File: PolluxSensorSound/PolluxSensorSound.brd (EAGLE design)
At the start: 100 x 80 mm, 0 parts

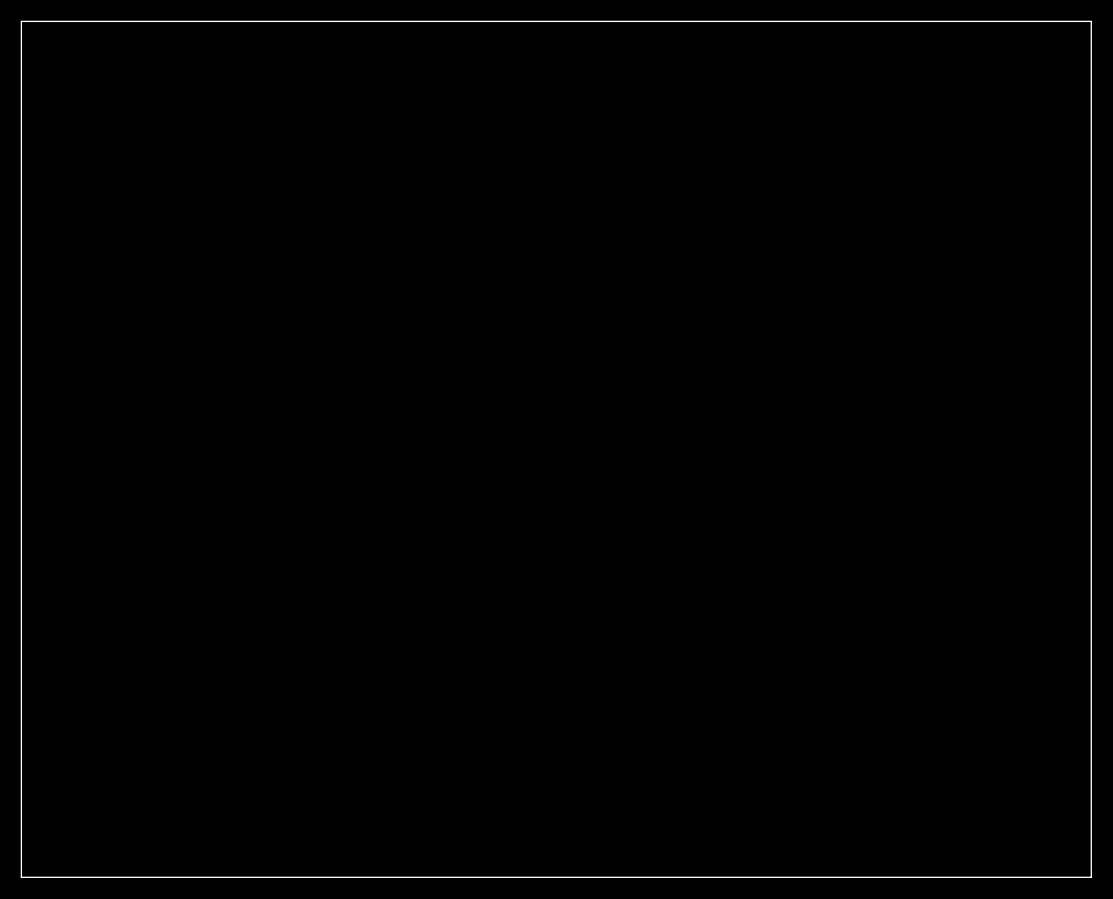
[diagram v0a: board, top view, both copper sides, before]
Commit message: add Temp sensor board and schematics
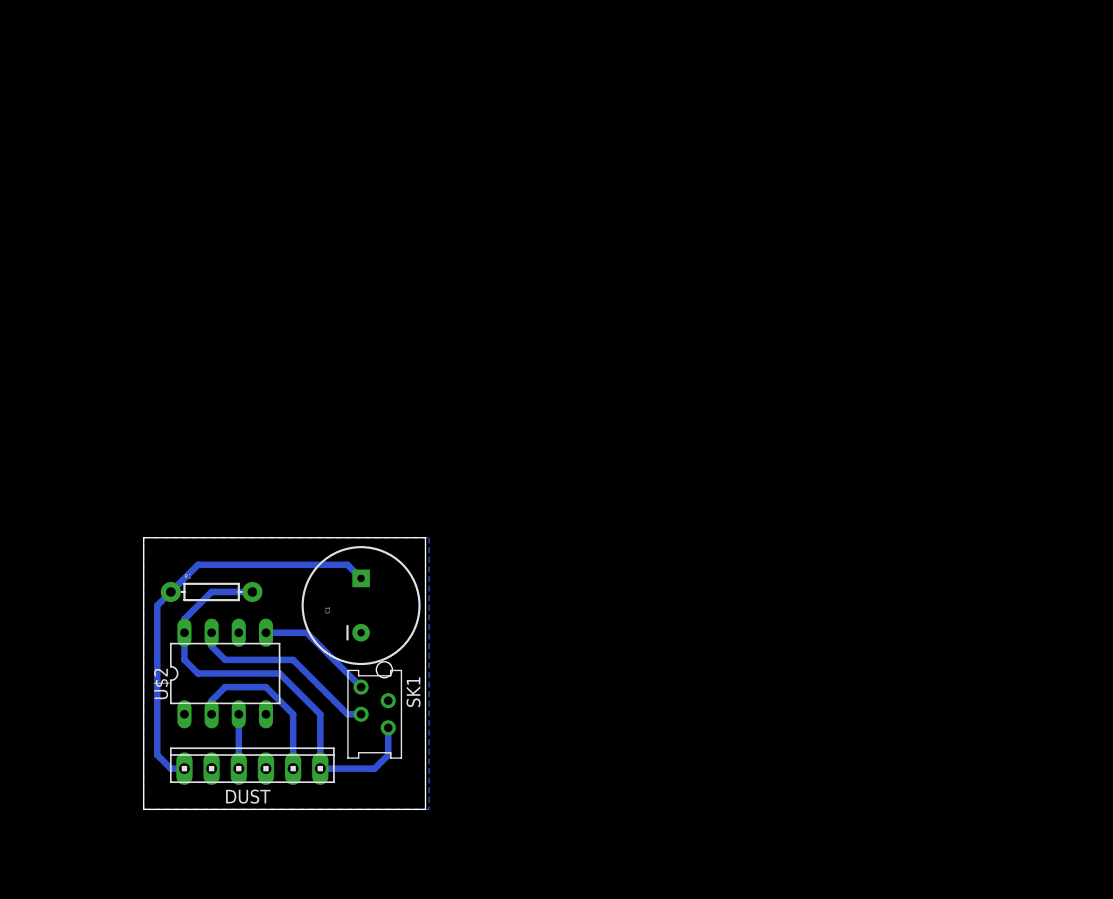
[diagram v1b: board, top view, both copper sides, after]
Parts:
- added C1: (no value), SparkFun:CPOL-RADIAL-1000UF-25V
- added DUST: (no value), con-amp:10X06MTA
- added R1: (no value), SparkFun:AXIAL-0.3
- added SK1: (no value), jt-con-micromatch:AMP-215079-8
- added U$2: TINY25/45/85-20PU, avr-7:DIL08
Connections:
- new net 5V: DUST.1, R1.P$2, SK1.4, U$2.8
- new net DUST_LED: DUST.4, U$2.3
- new net DUST_READ: DUST.2, U$2.2
- new net GND: C1.2, DUST.3, DUST.5, SK1.2, U$2.4
- new net N$1: SK1.3, U$2.7
- new net N$2: SK1.1, U$2.5
- new net N$4: C1.1, DUST.6, R1.P$1
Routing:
- net 5V: track 0.00 -> 40.5 mm
- net N$4: track 0.00 -> 38.2 mm
- net N$1: track 0.00 -> 17.9 mm
- net DUST_READ: track 0.00 -> 15.5 mm
- net N$2: track 0.00 -> 11.0 mm
- net DUST_LED: track 0.00 -> 5.08 mm
- added copper zone on layer 16, net GND
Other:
- board size 100 x 80 mm -> 26.3 x 25.4 mm
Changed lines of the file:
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@@
 <board>
 <plain>
-<wire x1="0" y1="0" x2="100" y2="0" width="0" layer="20"/>
-<wire x1="100" y1="0" x2="100" y2="80" width="0" layer="20"/>
-<wire x1="100" y1="80" x2="0" y2="80" width="0" layer="20"/>
-<wire x1="0" y1="80" x2="0" y2="0" width="0" layer="20"/>
+<wire x1="11.43" y1="6.35" x2="37.77" y2="6.35" width="0" layer="20"/>
+<wire x1="37.77" y1="6.35" x2="37.77" y2="31.74" width="0" layer="20"/>
+<wire x1="37.77" y1="31.74" x2="11.43" y2="31.74" width="0" layer="20"/>
+<wire x1="11.43" y1="31.74" x2="11.43" y2="6.35" width="0" layer="20"/>
 </plain>
 <attributes>
@@
 <param name="mtCopper" value="0.035mm 0.035mm 0.035mm 0.035mm 0.035mm 0.035mm 0.035mm 0.035mm 0.035mm 0.035mm 0.035mm 0.035mm 0.035mm 0.035mm 0.035mm 0.035mm"/>
 <param name="mtIsolate" value="1.5mm 0.15mm 0.2mm 0.15mm 0.2mm 0.15mm 0.2mm 0.15mm 0.2mm 0.15mm 0.2mm 0.15mm 0.2mm 0.15mm 0.2mm"/>
-<param name="mdWireWire" value="8mil"/>
-<param name="mdWirePad" value="8mil"/>
-<param name="mdWireVia" value="8mil"/>
+<param name="mdWireWire" value="24mil"/>
+<param name="mdWirePad" value="24mil"/>
+<param name="mdWireVia" value="24mil"/>
 <param name="mdPadPad" value="8mil"/>
 <param name="mdPadVia" value="8mil"/>
@@
 <param name="mdDrill" value="8mil"/>
 <param name="mdSmdStop" value="0mil"/>
-<param name="msWidth" value="10mil"/>
+<param name="msWidth" value="24mil"/>
 <param name="msDrill" value="24mil"/>
 <param name="msMicroVia" value="9.99mm"/>
@@
 </autorouter>
 <elements>
+<element name="SK1" library="jt-con-micromatch" package="AMP-215079-8" value="" x="33.02" y="17.78" rot="R270"/>
+<element name="U$2" library="avr-7" package="DIL08" value="TINY25/45/85-20PU" x="19.05" y="19.05"/>
+<element name="C1" library="SparkFun" package="CPOL-RADIAL-1000UF-25V" value="" x="31.75" y="25.4" rot="R90"/>
+<element name="R1" library="SparkFun" package="AXIAL-0.3" value="" x="17.78" y="26.67"/>
+<element name="DUST" library="con-amp" package="10X06MTA" value="" x="21.59" y="10.16"/>
 </elements>
 <signals>
+<signal name="N$2">
+<contactref element="SK1" pad="1"/>
+<contactref element="U$2" pad="5"/>
+<wire x1="22.86" y1="22.86" x2="26.67" y2="22.86" width="0.6096" layer="16"/>
+<wire x1="26.67" y1="22.86" x2="31.75" y2="17.78" width="0.6096" layer="16"/>
+</signal>
+<signal name="DUST_LED">
+<contactref element="DUST" pad="4"/>
+<contactref element="U$2" pad="3"/>
+<wire x1="20.32" y1="15.24" x2="20.32" y2="10.16" width="0.6096" layer="16"/>
+</signal>
+<signal name="5V">
+<contactref element="SK1" pad="4"/>
+<contactref element="U$2" pad="8"/>
+<contactref element="R1" pad="P$2"/>
+<contactref element="DUST" pad="1"/>
+<wire x1="15.24" y1="22.86" x2="15.24" y2="24.13" width="0.6096" layer="16"/>
+<wire x1="15.24" y1="24.13" x2="17.78" y2="26.67" width="0.6096" layer="16"/>
+<wire x1="17.78" y1="26.67" x2="21.59" y2="26.67" width="0.6096" layer="16"/>
+<wire x1="34.29" y1="13.97" x2="34.29" y2="11.43" width="0.6096" layer="16"/>
+<wire x1="34.29" y1="11.43" x2="33.02" y2="10.16" width="0.6096" layer="16"/>
+<wire x1="33.02" y1="10.16" x2="27.94" y2="10.16" width="0.6096" layer="16"/>
+<wire x1="27.94" y1="10.16" x2="27.94" y2="15.24" width="0.6096" layer="16"/>
+<wire x1="27.94" y1="15.24" x2="24.13" y2="19.05" width="0.6096" layer="16"/>
+<wire x1="24.13" y1="19.05" x2="16.51" y2="19.05" width="0.6096" layer="16"/>
+<wire x1="16.51" y1="19.05" x2="15.24" y2="20.32" width="0.6096" layer="16"/>
+<wire x1="15.24" y1="20.32" x2="15.24" y2="22.86" width="0.6096" layer="16"/>
+</signal>
+<signal name="GND">
+<contactref element="U$2" pad="4"/>
+<contactref element="SK1" pad="2"/>
+<contactref element="DUST" pad="5"/>
+<contactref element="C1" pad="2"/>
+<contactref element="DUST" pad="3"/>
+<polygon width="0.4064" layer="16" orphans="yes">
+<vertex x="11.43" y="31.75"/>
+<vertex x="38.1" y="31.75"/>
+<vertex x="38.1" y="6.35"/>
+<vertex x="11.43" y="6.35"/>
+</polygon>
+</signal>
+<signal name="N$1">
+<contactref element="U$2" pad="7"/>
+<contactref element="SK1" pad="3"/>
+<wire x1="17.78" y1="22.86" x2="17.78" y2="21.59" width="0.6096" layer="16"/>
+<wire x1="17.78" y1="21.59" x2="19.05" y2="20.32" width="0.6096" layer="16"/>
+<wire x1="19.05" y1="20.32" x2="25.4" y2="20.32" width="0.6096" layer="16"/>
+<wire x1="25.4" y1="20.32" x2="30.48" y2="15.24" width="0.6096" layer="16"/>
+<wire x1="30.48" y1="15.24" x2="31.75" y2="15.24" width="0.6096" layer="16"/>
+</signal>
+<signal name="DUST_READ">
+<contactref element="DUST" pad="2"/>
+<contactref element="U$2" pad="2"/>
+<wire x1="17.78" y1="15.24" x2="17.78" y2="16.51" width="0.6096" layer="16"/>
+<wire x1="17.78" y1="16.51" x2="19.05" y2="17.78" width="0.6096" layer="16"/>
+<wire x1="19.05" y1="17.78" x2="22.86" y2="17.78" width="0.6096" layer="16"/>
+<wire x1="22.86" y1="17.78" x2="25.4" y2="15.24" width="0.6096" layer="16"/>
+<wire x1="25.4" y1="15.24" x2="25.4" y2="10.16" width="0.6096" layer="16"/>
+</signal>
+<signal name="N$4">
+<contactref element="R1" pad="P$1"/>
+<contactref element="DUST" pad="6"/>
+<contactref element="C1" pad="1"/>
+<wire x1="15.24" y1="10.16" x2="13.97" y2="10.16" width="0.6096" layer="16"/>
+<wire x1="13.97" y1="10.16" x2="12.7" y2="11.43" width="0.6096" layer="16"/>
+<wire x1="12.7" y1="11.43" x2="12.7" y2="25.4" width="0.6096" layer="16"/>
+<wire x1="12.7" y1="25.4" x2="13.97" y2="26.67" width="0.6096" layer="16"/>
+<wire x1="13.97" y1="26.67" x2="16.51" y2="29.21" width="0.6096" layer="16"/>
+<wire x1="16.51" y1="29.21" x2="30.48" y2="29.21" width="0.6096" layer="16"/>
+<wire x1="30.48" y1="29.21" x2="31.75" y2="27.94" width="0.6096" layer="16"/>
+</signal>
 </signals>
 </board>

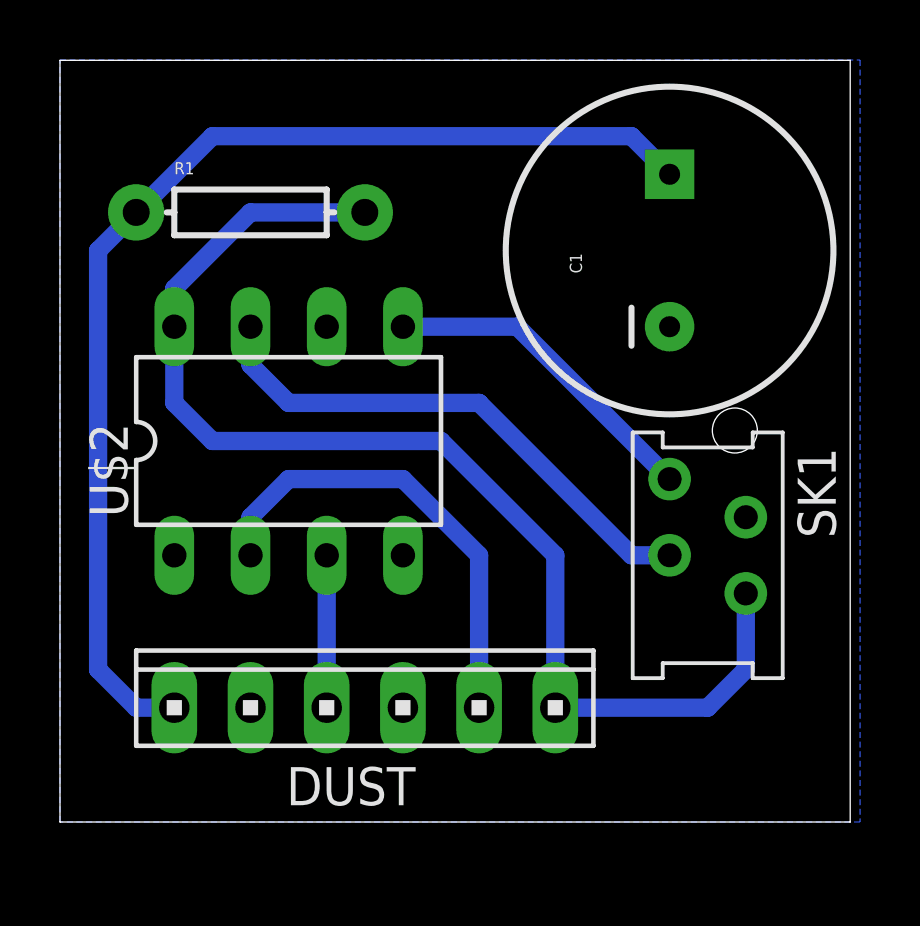
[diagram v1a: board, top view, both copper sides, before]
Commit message: add SPL sensor board and schematics
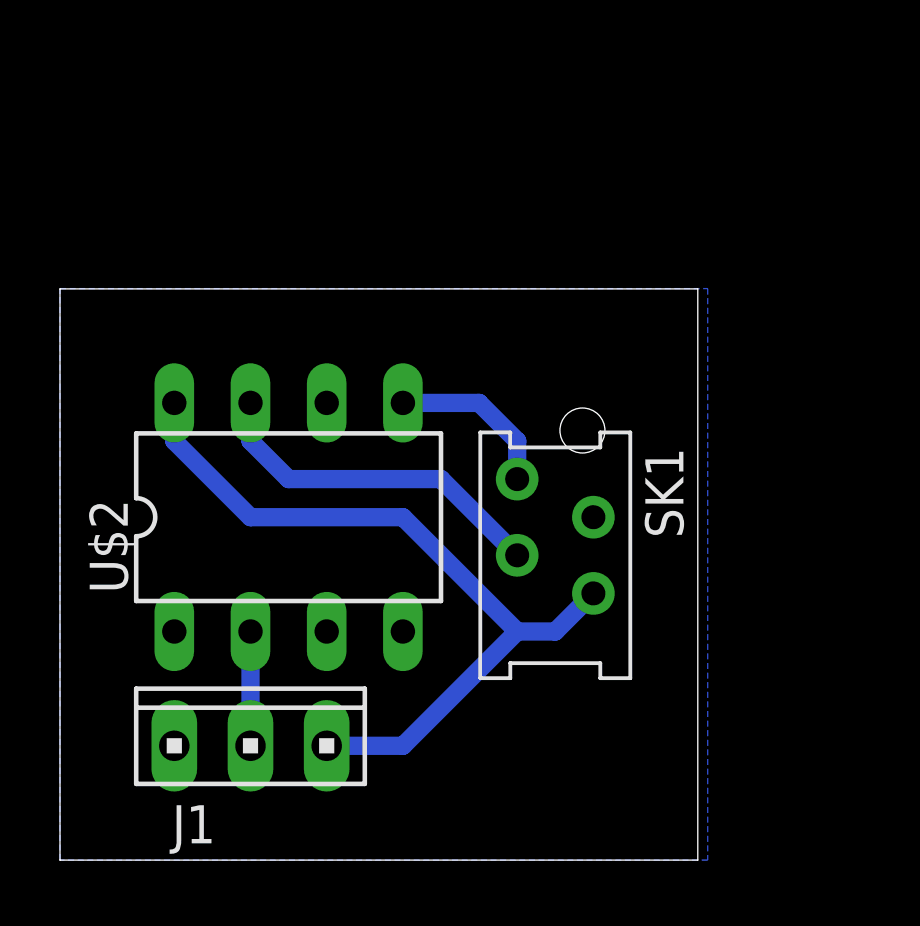
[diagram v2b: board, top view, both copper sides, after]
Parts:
- removed C1: (no value), SparkFun:CPOL-RADIAL-1000UF-25V
- removed DUST: (no value), con-amp:10X06MTA
- removed R1: (no value), SparkFun:AXIAL-0.3
- added J1: (no value), con-amp:10X03MTA
- moved SK1 5.08 mm to (27.9, 17.8)
- moved U$2 2.54 mm to (19.1, 16.5)
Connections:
- removed net DUST_LED: DUST.4, U$2.3
- removed net DUST_READ: DUST.2, U$2.2
- removed net N$4: C1.1, DUST.6, R1.P$1
- new net READ: J1.2, U$2.2
- net 5V: now also J1.1; no longer DUST.1, R1.P$2
- net GND: now also J1.3; no longer C1.2, DUST.3, DUST.5
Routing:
- net N$4: track 38.2 -> 0.00 mm
- net DUST_READ: track 15.5 -> 0.00 mm
- net 5V: track 40.5 -> 26.3 mm
- net N$1: track 17.9 -> 11.7 mm
- net N$2: track 11.0 -> 5.61 mm
- net DUST_LED: track 5.08 -> 0.00 mm
- net READ: track 0.00 -> 3.81 mm
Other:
- board size 26.3 x 25.4 mm -> 21.3 x 19 mm
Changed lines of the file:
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@@
 <board>
 <plain>
-<wire x1="11.43" y1="6.35" x2="37.77" y2="6.35" width="0" layer="20"/>
-<wire x1="37.77" y1="6.35" x2="37.77" y2="31.74" width="0" layer="20"/>
-<wire x1="37.77" y1="31.74" x2="11.43" y2="31.74" width="0" layer="20"/>
-<wire x1="11.43" y1="31.74" x2="11.43" y2="6.35" width="0" layer="20"/>
+<wire x1="11.43" y1="5.08" x2="32.69" y2="5.08" width="0" layer="20"/>
+<wire x1="32.69" y1="5.08" x2="32.69" y2="24.12" width="0" layer="20"/>
+<wire x1="32.69" y1="24.12" x2="11.43" y2="24.12" width="0" layer="20"/>
+<wire x1="11.43" y1="24.12" x2="11.43" y2="5.08" width="0" layer="20"/>
 </plain>
 <attributes>
@@
 </autorouter>
 <elements>
-<element name="SK1" library="jt-con-micromatch" package="AMP-215079-8" value="" x="33.02" y="17.78" rot="R270"/>
-<element name="U$2" library="avr-7" package="DIL08" value="TINY25/45/85-20PU" x="19.05" y="19.05"/>
-<element name="C1" library="SparkFun" package="CPOL-RADIAL-1000UF-25V" value="" x="31.75" y="25.4" rot="R90"/>
-<element name="R1" library="SparkFun" package="AXIAL-0.3" value="" x="17.78" y="26.67"/>
-<element name="DUST" library="con-amp" package="10X06MTA" value="" x="21.59" y="10.16"/>
+<element name="SK1" library="jt-con-micromatch" package="AMP-215079-8" value="" x="27.94" y="17.78" rot="R270"/>
+<element name="U$2" library="avr-7" package="DIL08" value="TINY25/45/85-20PU" x="19.05" y="16.51"/>
+<element name="J1" library="con-amp" package="10X03MTA" value="" x="17.78" y="8.89"/>
 </elements>
 <signals>
@@
 <contactref element="SK1" pad="1"/>
 <contactref element="U$2" pad="5"/>
-<wire x1="22.86" y1="22.86" x2="26.67" y2="22.86" width="0.6096" layer="16"/>
-<wire x1="26.67" y1="22.86" x2="31.75" y2="17.78" width="0.6096" layer="16"/>
-</signal>
-<signal name="DUST_LED">
-<contactref element="DUST" pad="4"/>
-<contactref element="U$2" pad="3"/>
-<wire x1="20.32" y1="15.24" x2="20.32" y2="10.16" width="0.6096" layer="16"/>
+<wire x1="22.86" y1="20.32" x2="25.4" y2="20.32" width="0.6096" layer="16"/>
+<wire x1="25.4" y1="20.32" x2="26.67" y2="19.05" width="0.6096" layer="16"/>
+<wire x1="26.67" y1="19.05" x2="26.67" y2="17.78" width="0.6096" layer="16"/>
 </signal>
 <signal name="5V">
 <contactref element="SK1" pad="4"/>
 <contactref element="U$2" pad="8"/>
-<contactref element="R1" pad="P$2"/>
-<contactref element="DUST" pad="1"/>
-<wire x1="15.24" y1="22.86" x2="15.24" y2="24.13" width="0.6096" layer="16"/>
-<wire x1="15.24" y1="24.13" x2="17.78" y2="26.67" width="0.6096" layer="16"/>
-<wire x1="17.78" y1="26.67" x2="21.59" y2="26.67" width="0.6096" layer="16"/>
-<wire x1="34.29" y1="13.97" x2="34.29" y2="11.43" width="0.6096" layer="16"/>
-<wire x1="34.29" y1="11.43" x2="33.02" y2="10.16" width="0.6096" layer="16"/>
-<wire x1="33.02" y1="10.16" x2="27.94" y2="10.16" width="0.6096" layer="16"/>
-<wire x1="27.94" y1="10.16" x2="27.94" y2="15.24" width="0.6096" layer="16"/>
-<wire x1="27.94" y1="15.24" x2="24.13" y2="19.05" width="0.6096" layer="16"/>
-<wire x1="24.13" y1="19.05" x2="16.51" y2="19.05" width="0.6096" layer="16"/>
-<wire x1="16.51" y1="19.05" x2="15.24" y2="20.32" width="0.6096" layer="16"/>
-<wire x1="15.24" y1="20.32" x2="15.24" y2="22.86" width="0.6096" layer="16"/>
+<contactref element="J1" pad="1"/>
+<wire x1="15.24" y1="20.32" x2="15.24" y2="19.05" width="0.6096" layer="16"/>
+<wire x1="15.24" y1="19.05" x2="17.78" y2="16.51" width="0.6096" layer="16"/>
+<wire x1="17.78" y1="16.51" x2="22.86" y2="16.51" width="0.6096" layer="16"/>
+<wire x1="22.86" y1="16.51" x2="26.67" y2="12.7" width="0.6096" layer="16"/>
+<wire x1="20.32" y1="8.89" x2="22.86" y2="8.89" width="0.6096" layer="16"/>
+<wire x1="22.86" y1="8.89" x2="26.67" y2="12.7" width="0.6096" layer="16"/>
+<wire x1="26.67" y1="12.7" x2="27.94" y2="12.7" width="0.6096" layer="16"/>
+<wire x1="27.94" y1="12.7" x2="29.21" y2="13.97" width="0.6096" layer="16"/>
 </signal>
 <signal name="GND">
 <contactref element="U$2" pad="4"/>
 <contactref element="SK1" pad="2"/>
-<contactref element="DUST" pad="5"/>
-<contactref element="C1" pad="2"/>
-<contactref element="DUST" pad="3"/>
 <polygon width="0.4064" layer="16" orphans="yes">
-<vertex x="11.43" y="31.75"/>
-<vertex x="38.1" y="31.75"/>
-<vertex x="38.1" y="6.35"/>
-<vertex x="11.43" y="6.35"/>
+<vertex x="11.43" y="24.13"/>
+<vertex x="33.02" y="24.13"/>
+<vertex x="33.02" y="5.08"/>
+<vertex x="11.43" y="5.08"/>
 </polygon>
+<contactref element="J1" pad="3"/>
 </signal>
 <signal name="N$1">
 <contactref element="U$2" pad="7"/>
 <contactref element="SK1" pad="3"/>
-<wire x1="17.78" y1="22.86" x2="17.78" y2="21.59" width="0.6096" layer="16"/>
-<wire x1="17.78" y1="21.59" x2="19.05" y2="20.32" width="0.6096" layer="16"/>
-<wire x1="19.05" y1="20.32" x2="25.4" y2="20.32" width="0.6096" layer="16"/>
-<wire x1="25.4" y1="20.32" x2="30.48" y2="15.24" width="0.6096" layer="16"/>
-<wire x1="30.48" y1="15.24" x2="31.75" y2="15.24" width="0.6096" layer="16"/>
-</signal>
-<signal name="DUST_READ">
-<contactref element="DUST" pad="2"/>
+<wire x1="17.78" y1="20.32" x2="17.78" y2="19.05" width="0.6096" layer="16"/>
+<wire x1="17.78" y1="19.05" x2="19.05" y2="17.78" width="0.6096" layer="16"/>
+<wire x1="19.05" y1="17.78" x2="24.13" y2="17.78" width="0.6096" layer="16"/>
+<wire x1="24.13" y1="17.78" x2="26.67" y2="15.24" width="0.6096" layer="16"/>
+</signal>
+<signal name="READ">
+<contactref element="J1" pad="2"/>
 <contactref element="U$2" pad="2"/>
-<wire x1="17.78" y1="15.24" x2="17.78" y2="16.51" width="0.6096" layer="16"/>
-<wire x1="17.78" y1="16.51" x2="19.05" y2="17.78" width="0.6096" layer="16"/>
-<wire x1="19.05" y1="17.78" x2="22.86" y2="17.78" width="0.6096" layer="16"/>
-<wire x1="22.86" y1="17.78" x2="25.4" y2="15.24" width="0.6096" layer="16"/>
-<wire x1="25.4" y1="15.24" x2="25.4" y2="10.16" width="0.6096" layer="16"/>
-</signal>
-<signal name="N$4">
-<contactref element="R1" pad="P$1"/>
-<contactref element="DUST" pad="6"/>
-<contactref element="C1" pad="1"/>
-<wire x1="15.24" y1="10.16" x2="13.97" y2="10.16" width="0.6096" layer="16"/>
-<wire x1="13.97" y1="10.16" x2="12.7" y2="11.43" width="0.6096" layer="16"/>
-<wire x1="12.7" y1="11.43" x2="12.7" y2="25.4" width="0.6096" layer="16"/>
-<wire x1="12.7" y1="25.4" x2="13.97" y2="26.67" width="0.6096" layer="16"/>
-<wire x1="13.97" y1="26.67" x2="16.51" y2="29.21" width="0.6096" layer="16"/>
-<wire x1="16.51" y1="29.21" x2="30.48" y2="29.21" width="0.6096" layer="16"/>
-<wire x1="30.48" y1="29.21" x2="31.75" y2="27.94" width="0.6096" layer="16"/>
+<wire x1="17.78" y1="12.7" x2="17.78" y2="8.89" width="0.6096" layer="16"/>
 </signal>
 </signals>

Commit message: improve sensor board
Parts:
- removed J1: (no value), con-amp:10X03MTA
- added C1: 1 uF, SparkFun:CPOL-RADIAL-10UF-25V
- added SOUND: (no value), pinhead-2:1X04M
- moved SK1 11.5 mm to (16.5, 16.5), turned to 90 degrees
- moved U$2 7.62 mm to (26.7, 16.5)
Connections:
- removed net N$2 (its old number): SK1.1, U$2.5
- new net SDA: SK1.4, U$2.5
- net 5V: now also C1.1, SK1.1, SOUND.3; no longer J1.1, SK1.4
- net GND: now also C1.2, SOUND.4; no longer J1.3
- net READ: now also SOUND.1; no longer J1.2
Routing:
- net SDA: track 0.00 -> 20.6 mm
- net READ: track 3.81 -> 19.5 mm
- net 5V: track 26.3 -> 40.7 mm
- net N$2 (its old number): track 5.61 -> 0.00 mm
- net N$2: track 11.7 -> 12.5 mm
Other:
- board size 21.3 x 19 mm -> 32.7 x 17.8 mm
